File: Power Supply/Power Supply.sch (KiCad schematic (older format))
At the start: 30 parts, among them J1 Conn_01x01_Female, J2 Conn_01x01_Female, J3 Conn_01x01_Female, J4 Conn_01x01_Female, J5 Conn_01x01_Female, U1 LM337_TO220, U2 LM317_3PinPackage

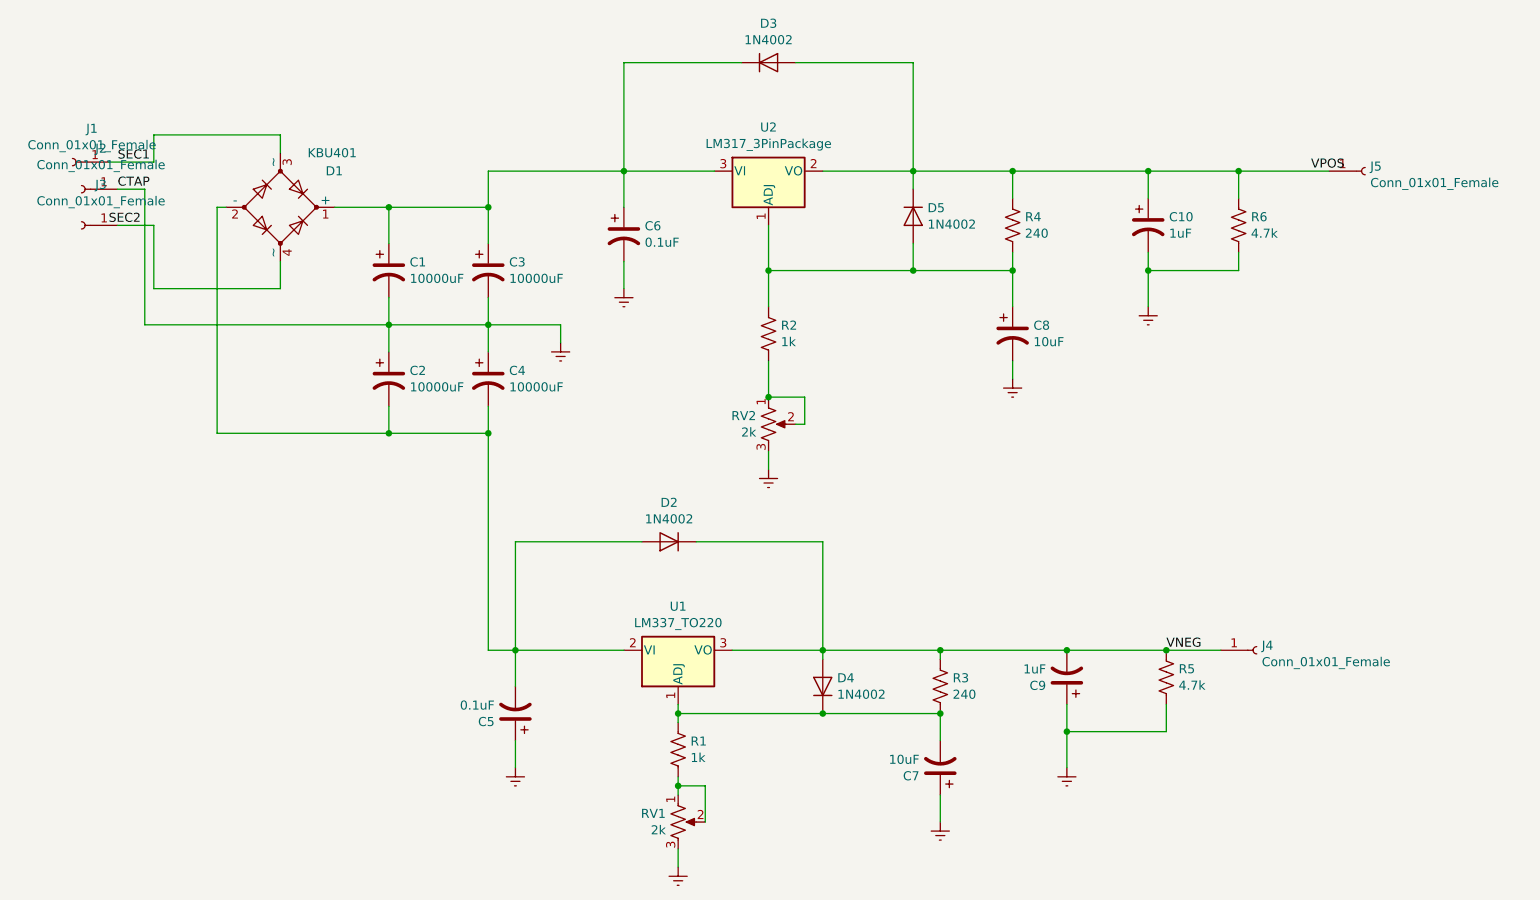
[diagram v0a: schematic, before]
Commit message: cleaned up pcb, fixed bridge rectifier pinout, added silkscreen and exported fabrication files
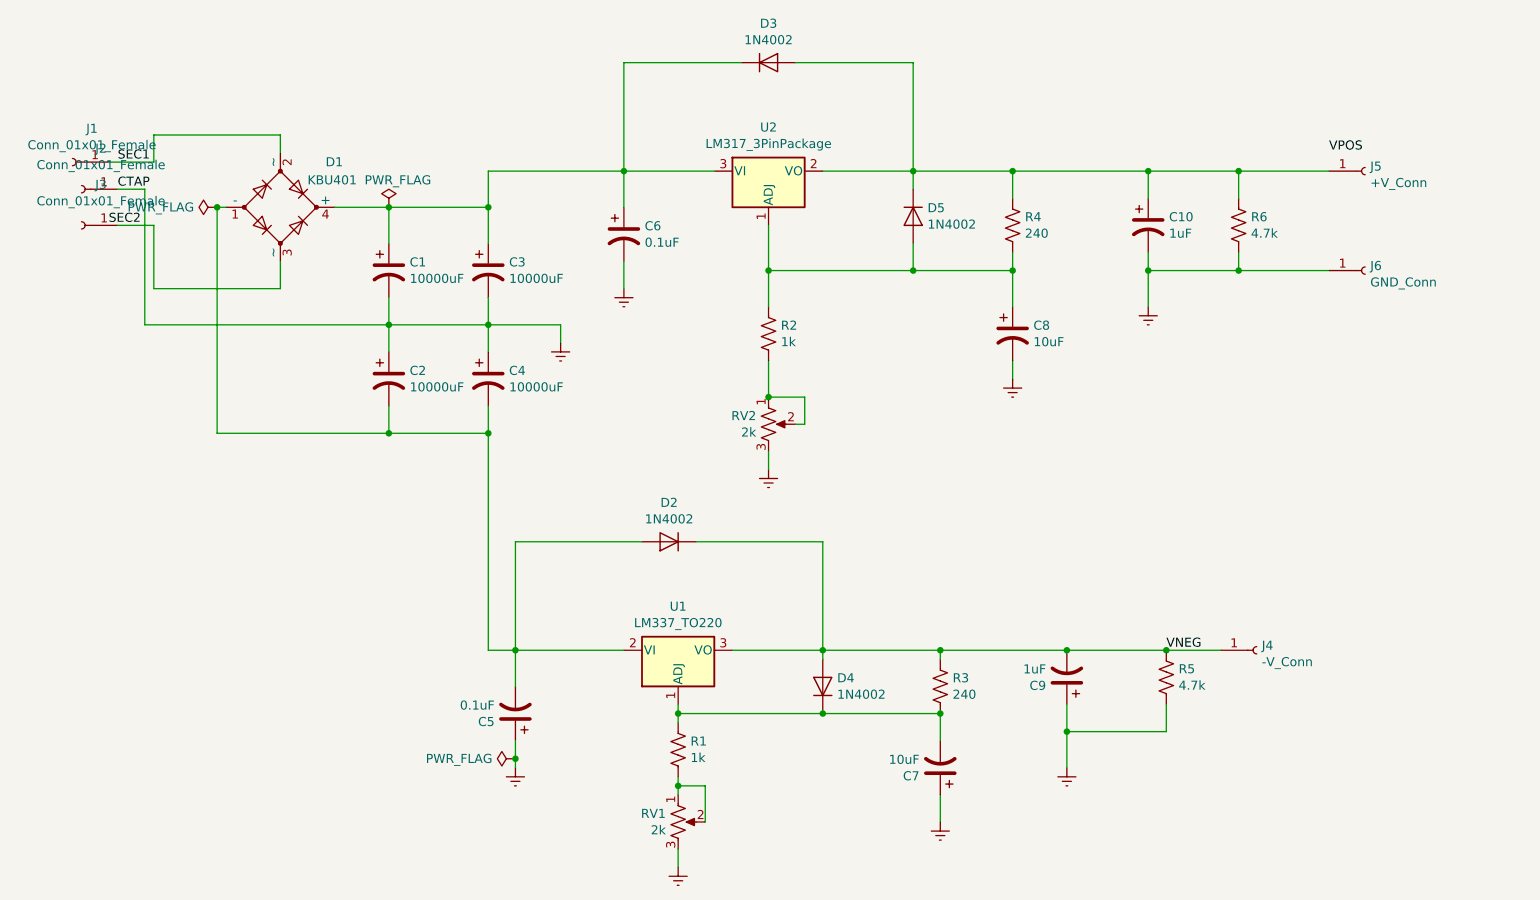
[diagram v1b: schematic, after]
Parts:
- removed D1: KBU401, Diode_THT:Diode_Bridge_Vishay_KBU, symbol Device:D_Bridge_+-AA
- added D1: KBU401, Diode_THT:Diode_Bridge_Vishay_KBU, symbol Device:D_Bridge_-AA+
- added J6: GND_Conn, Connector_Pin:Pin_D1.1mm_L10.2mm_W3.5mm_Flat, symbol Connector:Conn_01x01_Female
- J4: value Conn_01x01_Female -> -V_Conn
- J5: value Conn_01x01_Female -> +V_Conn
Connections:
- net Earth: now also J6.1 (Pin_1)
- net SEC1: now also D1.2 (~~)
- net VPOS: no longer C10.1, D3.2 (A), D5.1 (K), J5.1 (Pin_1), R4.1, R6.1, U2.2 (VO)
- net at C1.1, C3.1, C6.1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: now also D1.4 (+)
- net at C2.2, C4.2, C5.2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: now also D1.1 (-)
- net at J3.1 (Pin_1): now also D1.3 (~~)
- new net: C10.1, D3.2 (A), D5.1 (K), J5.1 (Pin_1), R4.1, R6.1, U2.2 (VO)
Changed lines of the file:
@@
 $EndDescr
-$Comp
-L Device:D_Bridge_+-AA D1
-U 1 1 5F56E05F
-P 1750 1900
-F 0 "D1" H 2000 2100 50  0000 L CNN
-F 1 "KBU401" H 1900 2200 50  0000 L CNN
-F 2 "Diode_THT:Diode_Bridge_Vishay_KBU" H 1750 1900 50  0001 C CNN
-F 3 "~" H 1750 1900 50  0001 C CNN
-	1    1750 1900
-	1    0    0    -1
-$EndComp
 $Comp
 L Device:CP1 C1
@@
 	7050 1700 7550 1700
 Connection ~ 7050 1700
-Text Label 7450 1700 0    50   ~ 0
+Text Label 7550 1600 0    50   ~ 0
 VPOS
 Connection ~ 4450 2950
@@
 	3050 4350 3050 4550
 Wire Wire Line
-	3050 5000 3050 4850
+	3050 5000 3050 4950
 Wire Wire Line
 	3950 5150 3950 5100
@@
 P 7750 1700
 F 0 "J5" H 7778 1726 50  0000 L CNN
-F 1 "Conn_01x01_Female" H 7778 1635 50  0000 L CNN
+F 1 "+V_Conn" H 7778 1635 50  0000 L CNN
 F 2 "Connector_Pin:Pin_D1.1mm_L10.2mm_W3.5mm_Flat" H 7750 1700 50  0001 C CNN
 F 3 "~" H 7750 1700 50  0001 C CNN
@@
 P 7150 4350
 F 0 "J4" H 7178 4376 50  0000 L CNN
-F 1 "Conn_01x01_Female" H 7178 4285 50  0000 L CNN
+F 1 "-V_Conn" H 7178 4285 50  0000 L CNN
 F 2 "Connector_Pin:Pin_D1.1mm_L10.2mm_W3.5mm_Flat" H 7150 4350 50  0001 C CNN
 F 3 "~" H 7150 4350 50  0001 C CNN
@@
 Wire Wire Line
 	3650 1700 4150 1700
+$Comp
+L Connector:Conn_01x01_Female J6
+U 1 1 5FFF08B4
+P 7750 2250
+F 0 "J6" H 7778 2276 50  0000 L CNN
+F 1 "GND_Conn" H 7778 2185 50  0000 L CNN
+F 2 "Connector_Pin:Pin_D1.1mm_L10.2mm_W3.5mm_Flat" H 7750 2250 50  0001 C CNN
+F 3 "~" H 7750 2250 50  0001 C CNN
+	1    7750 2250
+	1    0    0    -1
+$EndComp
+Wire Wire Line
+	7550 2250 7050 2250
+Connection ~ 7050 2250
+$Comp
+L Device:D_Bridge_-AA+ D1
+U 1 1 5FFF44BB
+P 1750 1900
+F 0 "D1" H 2000 2150 50  0000 L CNN
+F 1 "KBU401" H 1900 2050 50  0000 L CNN
+F 2 "Diode_THT:Diode_Bridge_Vishay_KBU" H 1750 1900 50  0001 C CNN
+F 3 "~" H 1750 1900 50  0001 C CNN
+	1    1750 1900
+	1    0    0    -1
+$EndComp
+$Comp
+L power:PWR_FLAG #FLG0101
+U 1 1 5FFFA6FC
+P 3050 4950
+F 0 "#FLG0101" H 3050 5025 50  0001 C CNN
+F 1 "PWR_FLAG" V 3050 5077 50  0000 L CNN
+F 2 "" H 3050 4950 50  0001 C CNN
+F 3 "~" H 3050 4950 50  0001 C CNN
+	1    3050 4950
+	0    -1   -1   0
+$EndComp
+Connection ~ 3050 4950
+Wire Wire Line
+	3050 4950 3050 4850
+$Comp
+L power:PWR_FLAG #FLG0102
+U 1 1 5FFFB313
+P 1400 1900
+F 0 "#FLG0102" H 1400 1975 50  0001 C CNN
+F 1 "PWR_FLAG" V 1400 2027 50  0000 L CNN
+F 2 "" H 1400 1900 50  0001 C CNN
+F 3 "~" H 1400 1900 50  0001 C CNN
+	1    1400 1900
+	0    -1   -1   0
+$EndComp
+Connection ~ 1400 1900
+$Comp
+L power:PWR_FLAG #FLG0103
+U 1 1 5FFFB8C8
+P 2350 1900
+F 0 "#FLG0103" H 2350 1975 50  0001 C CNN
+F 1 "PWR_FLAG" H 2400 2050 50  0000 C CNN
+F 2 "" H 2350 1900 50  0001 C CNN
+F 3 "~" H 2350 1900 50  0001 C CNN
+	1    2350 1900
+	1    0    0    -1
+$EndComp
 $EndSCHEMATC
